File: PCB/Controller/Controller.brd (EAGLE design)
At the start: 30 x 30 mm, 20 parts

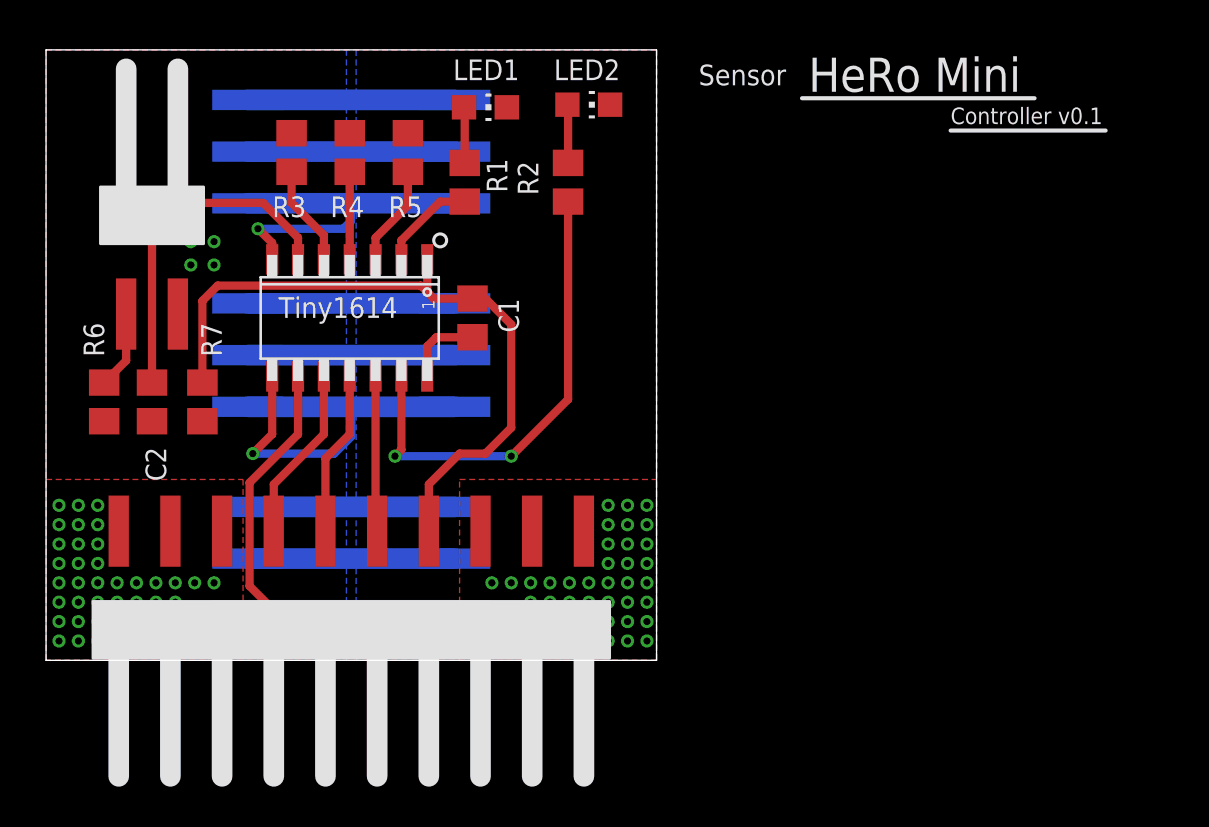
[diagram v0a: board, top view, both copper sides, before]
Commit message: Changed PCB size to 25mmx25mm
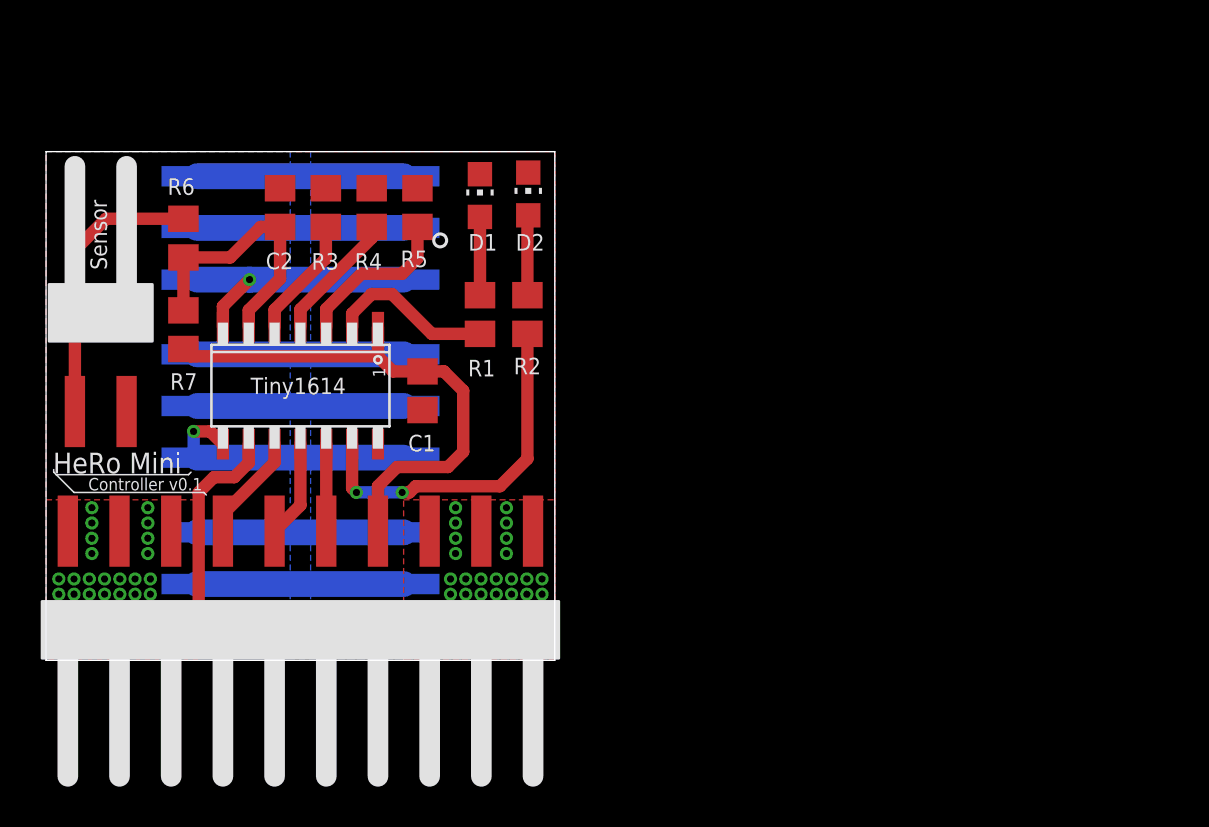
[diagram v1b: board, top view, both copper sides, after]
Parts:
- removed LED1, LED2: GREEN, led:CHIP-LED0805
- added D1, D2: GREEN, led:CHIP-LED0805
- moved C2 11.4 mm to (11.5, 22.2), turned to 90 degrees
- moved R6 8.94 mm to (6.75, 20.8)
- moved R2 6.80 mm to (23.7, 17.0)
- moved R1 6.54 mm to (21.3, 17.0)
- moved U$5 5.41 mm to (2.69, 17.3)
- moved U$1 4.51 mm to (12.5, 21.2)
- moved U$6 4.51 mm to (12.5, 21.2)
- moved C1 4.34 mm to (18.5, 13.2)
- moved LEG_0 4.12 mm to (12.5, 13.5)
- moved R7 3.67 mm to (6.75, 16.2), turned to 270 degrees
- moved U$2 3.54 mm to (12.5, 12.5)
- moved U$7 3.54 mm to (12.5, 12.5)
- moved R3 3.19 mm to (13.8, 22.2)
- moved R4 2.91 mm to (16.0, 22.2)
- moved U$3 2.80 mm to (12.5, 3.75)
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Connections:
- net GND: now also D1.C, D2.C; no longer LED1.C, LED2.C
- net N$1: now also D1.A; no longer LED1.A
- net N$2: now also D2.A; no longer LED2.A
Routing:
- net N$4: track 3.82 -> 13.9 mm
- net +5V: track 34.5 -> 26.1 mm
- net PWMB_0: track 21.0 -> 13.2 mm
- net LEDB_0: track 23.4 -> 17.7 mm
- net PWMC_0: track 17.6 -> 13.0 mm
- net GND: track 34.4 -> 30.5 mm, vias 48 -> 43
- net SENSE_0: track 17.4 -> 13.5 mm
- net SCL: track 7.63 -> 4.28 mm
- net LEDA_0: track 4.84 -> 8.16 mm
- net UPDI_0: track 8.62 -> 5.33 mm
- net SDA: track 8.10 -> 4.80 mm
- net ADDC_0: track 4.96 -> 7.95 mm
- net ADDB_0: track 4.30 -> 6.37 mm
- net PWMA_0: track 27.0 -> 25.9 mm
- net N$1: track 2.75 -> 3.85 mm
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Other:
- board size 30 x 30 mm -> 25 x 25 mm

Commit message: Minor Changes
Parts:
- removed D1, D2: GREEN, led:CHIP-LED0805
- added LED: DUO_LED, HeRo:DUO_LED
- moved R1 0.38 mm to (20.9, 17.0)
- moved R2 0.38 mm to (23.3, 17.0)
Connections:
- net GND: now also LED.CG, LED.CR; no longer D1.C, D2.C
- net N$1: now also LED.AG; no longer D1.A
- net N$2: now also LED.AR; no longer D2.A
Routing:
- net N$2: track 3.94 -> 2.59 mm
- net N$1: track 3.85 -> 2.60 mm
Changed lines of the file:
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@@
 <?xml version="1.0" encoding="utf-8"?>
 <!DOCTYPE eagle SYSTEM "eagle.dtd">
-<eagle version="9.0.0">
+<eagle version="8.7.0">
 <drawing>
 <settings>
@@
 <setting verticaltext="up"/>
 </settings>
-<grid distance="2" unitdist="mm" unit="mm" style="lines" multiple="1" display="no" altdistance="0.125" altunitdist="mm" altunit="mm"/>
+<grid distance="78.7401575" unitdist="mil" unit="mil" style="lines" multiple="1" display="no" altdistance="4.92125984" altunitdist="mil" altunit="mil"/>
 <layers>
 <layer number="1" name="Top" color="4" fill="1" visible="yes" active="yes"/>
@@
 <layer number="20" name="Dimension" color="24" fill="1" visible="yes" active="yes"/>
 <layer number="21" name="tPlace" color="7" fill="1" visible="yes" active="yes"/>
-<layer number="22" name="bPlace" color="7" fill="1" visible="no" active="yes"/>
+<layer number="22" name="bPlace" color="7" fill="1" visible="yes" active="yes"/>
 <layer number="23" name="tOrigins" color="15" fill="1" visible="yes" active="yes"/>
-<layer number="24" name="bOrigins" color="15" fill="1" visible="no" active="yes"/>
+<layer number="24" name="bOrigins" color="15" fill="1" visible="yes" active="yes"/>
 <layer number="25" name="tNames" color="7" fill="1" visible="yes" active="yes"/>
-<layer number="26" name="bNames" color="7" fill="1" visible="no" active="yes"/>
-<layer number="27" name="tValues" color="7" fill="1" visible="no" active="yes"/>
-<layer number="28" name="bValues" color="7" fill="1" visible="no" active="yes"/>
+<layer number="26" name="bNames" color="7" fill="1" visible="yes" active="yes"/>
+<layer number="27" name="tValues" color="7" fill="1" visible="yes" active="yes"/>
+<layer number="28" name="bValues" color="7" fill="1" visible="yes" active="yes"/>
 <layer number="29" name="tStop" color="7" fill="3" visible="no" active="yes"/>
 <layer number="30" name="bStop" color="7" fill="6" visible="no" active="yes"/>
@@
 <layer number="38" name="bTest" color="7" fill="1" visible="no" active="yes"/>
 <layer number="39" name="tKeepout" color="4" fill="11" visible="yes" active="yes"/>
-<layer number="40" name="bKeepout" color="1" fill="11" visible="no" active="yes"/>
+<layer number="40" name="bKeepout" color="1" fill="11" visible="yes" active="yes"/>
 <layer number="41" name="tRestrict" color="4" fill="10" visible="yes" active="yes"/>
-<layer number="42" name="bRestrict" color="1" fill="10" visible="no" active="yes"/>
+<layer number="42" name="bRestrict" color="1" fill="10" visible="yes" active="yes"/>
 <layer number="43" name="vRestrict" color="2" fill="10" visible="no" active="yes"/>
-<layer number="44" name="Drills" color="7" fill="1" visible="no" active="yes"/>
+<layer number="44" name="Drills" color="7" fill="1" visible="yes" active="yes"/>
 <layer number="45" name="Holes" color="7" fill="1" visible="yes" active="yes"/>
 <layer number="46" name="Milling" color="3" fill="1" visible="no" active="yes"/>
@@
 <layer number="49" name="Reference" color="7" fill="1" visible="no" active="yes"/>
 <layer number="51" name="tDocu" color="7" fill="1" visible="yes" active="yes"/>
-<layer number="52" name="bDocu" color="7" fill="1" visible="no" active="yes"/>
+<layer number="52" name="bDocu" color="7" fill="1" visible="yes" active="yes"/>
 <layer number="88" name="SimResults" color="9" fill="1" visible="no" active="no"/>
 <layer number="89" name="SimProbes" color="9" fill="1" visible="no" active="no"/>
@@
 <attribute name="SPICEPREFIX" value="C" x="18.5" y="13.25" size="1.778" layer="27" rot="R270" display="off"/>
 </element>
-<element name="R1" library="rcl" library_urn="urn:adsk.eagle:library:334" package="R0805" package3d_urn="urn:adsk.eagle:package:23553/2" value="680" x="21.324" y="16.995" smashed="yes" rot="R90">
-<attribute name="NAME" x="20.737" y="13.9555" size="0.8128" layer="25"/>
-<attribute name="SPICEPREFIX" value="R" x="21.324" y="16.995" size="1.778" layer="27" rot="R90" display="off"/>
-</element>
-<element name="R2" library="rcl" library_urn="urn:adsk.eagle:library:334" package="R0805" package3d_urn="urn:adsk.eagle:package:23553/2" value="680" x="23.654" y="16.995" smashed="yes" rot="R90">
-<attribute name="NAME" x="22.985" y="14.0565" size="0.8128" layer="25"/>
-<attribute name="SPICEPREFIX" value="R" x="23.654" y="16.995" size="1.778" layer="27" rot="R90" display="off"/>
-</element>
-<element name="D1" library="led" library_urn="urn:adsk.eagle:library:259" package="CHIP-LED0805" package3d_urn="urn:adsk.eagle:package:15818/2" value="GREEN" x="21.322" y="22.84" smashed="yes">
-<attribute name="NAME" x="20.7525" y="20.1365" size="0.8128" layer="25"/>
-<attribute name="SPICEPREFIX" value="L" x="21.322" y="22.84" size="1.778" layer="27" display="off"/>
-</element>
-<element name="D2" library="led" library_urn="urn:adsk.eagle:library:259" package="CHIP-LED0805" package3d_urn="urn:adsk.eagle:package:15818/2" value="GREEN" x="23.695" y="22.92" smashed="yes">
-<attribute name="NAME" x="23.0805" y="20.1365" size="0.8128" layer="25"/>
-<attribute name="SPICEPREFIX" value="L" x="23.695" y="22.92" size="1.778" layer="27" display="off"/>
+<element name="R1" library="rcl" library_urn="urn:adsk.eagle:library:334" package="R0805" package3d_urn="urn:adsk.eagle:package:23553/2" value="680" x="20.949" y="16.995" smashed="yes" rot="R90">
+<attribute name="NAME" x="20.362" y="13.9555" size="0.8128" layer="25"/>
+<attribute name="SPICEPREFIX" value="R" x="20.949" y="16.995" size="1.778" layer="27" rot="R90" display="off"/>
+</element>
+<element name="R2" library="rcl" library_urn="urn:adsk.eagle:library:334" package="R0805" package3d_urn="urn:adsk.eagle:package:23553/2" value="680" x="23.279" y="16.995" smashed="yes" rot="R90">
+<attribute name="NAME" x="22.61" y="14.0565" size="0.8128" layer="25"/>
+<attribute name="SPICEPREFIX" value="R" x="23.279" y="16.995" size="1.778" layer="27" rot="R90" display="off"/>
 </element>
 <element name="R3" library="rcl" library_urn="urn:adsk.eagle:library:334" package="R0805" package3d_urn="urn:adsk.eagle:package:23553/2" value="10k" x="13.75" y="22.25" smashed="yes" rot="R90">
@@
 <attribute name="NAME" x="6.0975" y="13.2975" size="0.8128" layer="25"/>
 <attribute name="SPICEPREFIX" value="R" x="6.75" y="16.25" size="1.778" layer="27" rot="R270" display="off"/>
+</element>
+<element name="LED" library="HeRo" package="DUO_LED" value="DUO_LED" x="22.125" y="21.75" smashed="yes" rot="R270">
+<attribute name="NAME" x="19.585" y="24.29" size="0.8128" layer="25" rot="R270"/>
+<attribute name="VALUE" x="18.315" y="24.29" size="0.8128" layer="27" rot="R270"/>
 </element>
 </elements>
@@
 <signal name="GND">
 <contactref element="LEG_0" pad="14"/>
-<contactref element="D1" pad="C"/>
-<contactref element="D2" pad="C"/>
 <contactref element="R3" pad="2"/>
 <contactref element="R4" pad="2"/>
@@
 <via x="5.125" y="1.75" extent="1-16" drill="0.35" shape="octagon"/>
 <via x="5.125" y="1" extent="1-16" drill="0.35" shape="octagon"/>
+<contactref element="LED" pad="CR"/>
+<contactref element="LED" pad="CG"/>
 </signal>
 <signal name="UPDI_0">
@@
 <contactref element="LEG_0" pad="11"/>
 <contactref element="U$4" pad="6"/>
-<wire x1="12.5" y1="10.625" x2="12.5" y2="7.62" width="0.6096" layer="1"/>
-<wire x1="12.5" y1="7.62" x2="11.23" y2="6.35" width="0.6096" layer="1"/>
+<wire x1="12.5" y1="10.625" x2="12.5" y2="9.25" width="0.6096" layer="1"/>
+<wire x1="12.5" y1="9.25" x2="11.25" y2="8" width="0.6096" layer="1"/>
+<wire x1="11.25" y1="8" x2="11.25" y2="6.37" width="0.6096" layer="1"/>
+<wire x1="11.25" y1="6.37" x2="11.23" y2="6.35" width="0.6096" layer="1"/>
 </signal>
 <signal name="SCL">
@@
 <wire x1="17.5" y1="8.25" x2="17.85681875" y2="8.25" width="0.6096" layer="1"/>
 <wire x1="17.85681875" y1="8.25" x2="18.16161875" y2="8.5548" width="0.6096" layer="1"/>
-<wire x1="18.16161875" y1="8.5548" x2="22.3048" y2="8.5548" width="0.6096" layer="1"/>
-<wire x1="23.654" y1="9.904" x2="23.654" y2="16.045" width="0.6096" layer="1"/>
-<wire x1="22.3048" y1="8.5548" x2="23.654" y2="9.904" width="0.6096" layer="1"/>
+<wire x1="18.16161875" y1="8.5548" x2="21.9298" y2="8.5548" width="0.6096" layer="1"/>
+<wire x1="23.279" y1="9.904" x2="23.279" y2="16.045" width="0.6096" layer="1"/>
+<wire x1="21.9298" y1="8.5548" x2="23.279" y2="9.904" width="0.6096" layer="1"/>
 </signal>
 <signal name="LEDA_0">
@@
 <wire x1="15.04" y1="17.04" x2="16" y2="18" width="0.6096" layer="1"/>
 <wire x1="16" y1="18" x2="17" y2="18" width="0.6096" layer="1"/>
-<wire x1="18.955" y1="16.045" x2="21.324" y2="16.045" width="0.6096" layer="1"/>
+<wire x1="18.955" y1="16.045" x2="20.949" y2="16.045" width="0.6096" layer="1"/>
 <wire x1="17" y1="18" x2="18.955" y2="16.045" width="0.6096" layer="1"/>
 </signal>
@@
 <signal name="N$1">
 <contactref element="R1" pad="2"/>
-<contactref element="D1" pad="A"/>
-<wire x1="21.324" y1="17.945" x2="21.324" y2="21.788" width="0.6096" layer="1"/>
-<wire x1="21.324" y1="21.788" x2="21.322" y2="21.79" width="0.6096" layer="1"/>
+<contactref element="LED" pad="AG"/>
+<wire x1="20.949" y1="17.945" x2="21.3" y2="18.296" width="0.6096" layer="1"/>
+<wire x1="21.3" y1="18.296" x2="21.3" y2="20.4" width="0.6096" layer="1"/>
 </signal>
 <signal name="N$2">
 <contactref element="R2" pad="2"/>
-<contactref element="D2" pad="A"/>
-<wire x1="23.654" y1="17.945" x2="23.654" y2="21.829" width="0.6096" layer="1"/>
-<wire x1="23.654" y1="21.829" x2="23.695" y2="21.87" width="0.6096" layer="1"/>
+<contactref element="LED" pad="AR"/>
+<wire x1="23.279" y1="17.945" x2="22.95" y2="18.274" width="0.6096" layer="1"/>
+<wire x1="22.95" y1="18.274" x2="22.95" y2="20.4" width="0.6096" layer="1"/>
 </signal>
 <signal name="N$4">

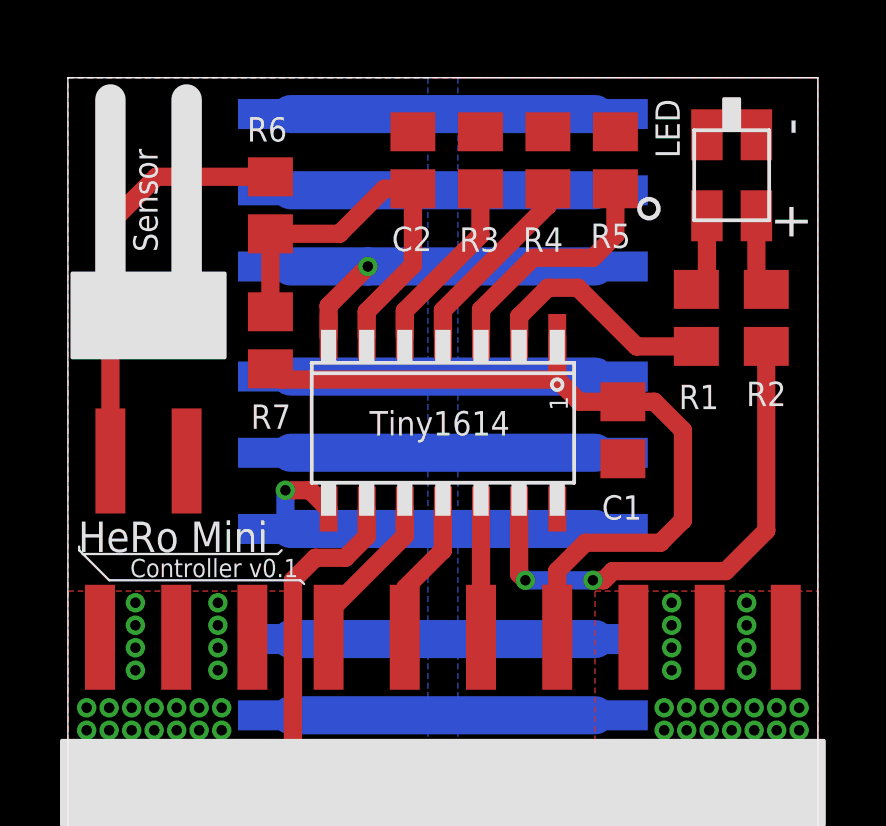
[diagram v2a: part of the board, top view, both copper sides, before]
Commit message: finalised routing, added 3D-Models
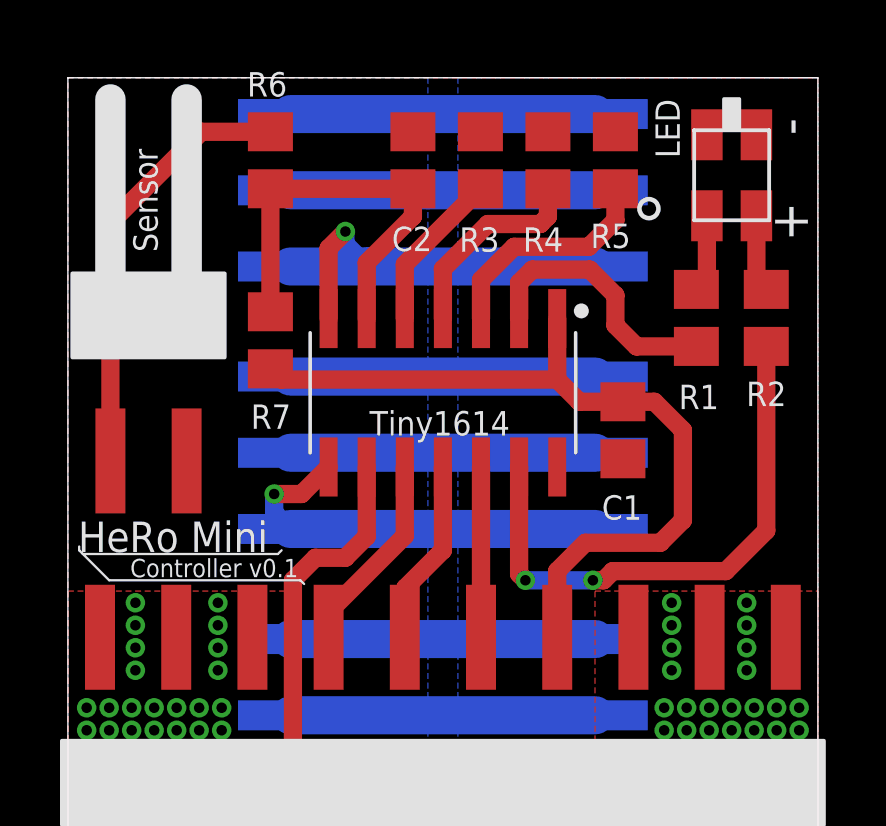
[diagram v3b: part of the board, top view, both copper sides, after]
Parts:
- LEG_0: value ATTINY1614 -> ATTINY16142; device HeRo:SOIC14 -> HeRo:SOIC127P600X175-14
- moved R6 1.50 mm to (6.75, 22.2)
- moved LEG_0 1.00 mm to (12.5, 14.5), turned to 270 degrees
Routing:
- net PWMC_0: track 13.0 -> 14.8 mm
- net PWMA_0: track 25.9 -> 27.3 mm
- net LEDB_0: track 17.3 -> 18.7 mm
- net UPDI_0: track 5.33 -> 6.73 mm
- net SDA: track 4.80 -> 6.20 mm
- net SCL: track 4.28 -> 5.68 mm
- net LEDA_0: track 7.78 -> 8.93 mm
- net N$4: track 13.9 -> 14.5 mm
- net ADDA_0: track 5.97 -> 5.37 mm
- net +5V: track 26.1 -> 26.7 mm
- net PWMB_0: track 13.2 -> 13.7 mm
